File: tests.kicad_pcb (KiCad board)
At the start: 2 copper layers, 30 x 20 mm, 7 parts, among them J101 USB_A+C+XT30

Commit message: ...
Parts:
- moved TP104 2.00 mm to (95.0, 97.0)
- moved TP105 2.00 mm to (95.0, 95.0)
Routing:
- net /SBU1: track 14.8 -> 15.6 mm, vias 0 -> 1
- net /CC2: track 15.2 -> 14.6 mm, vias 1 -> 0

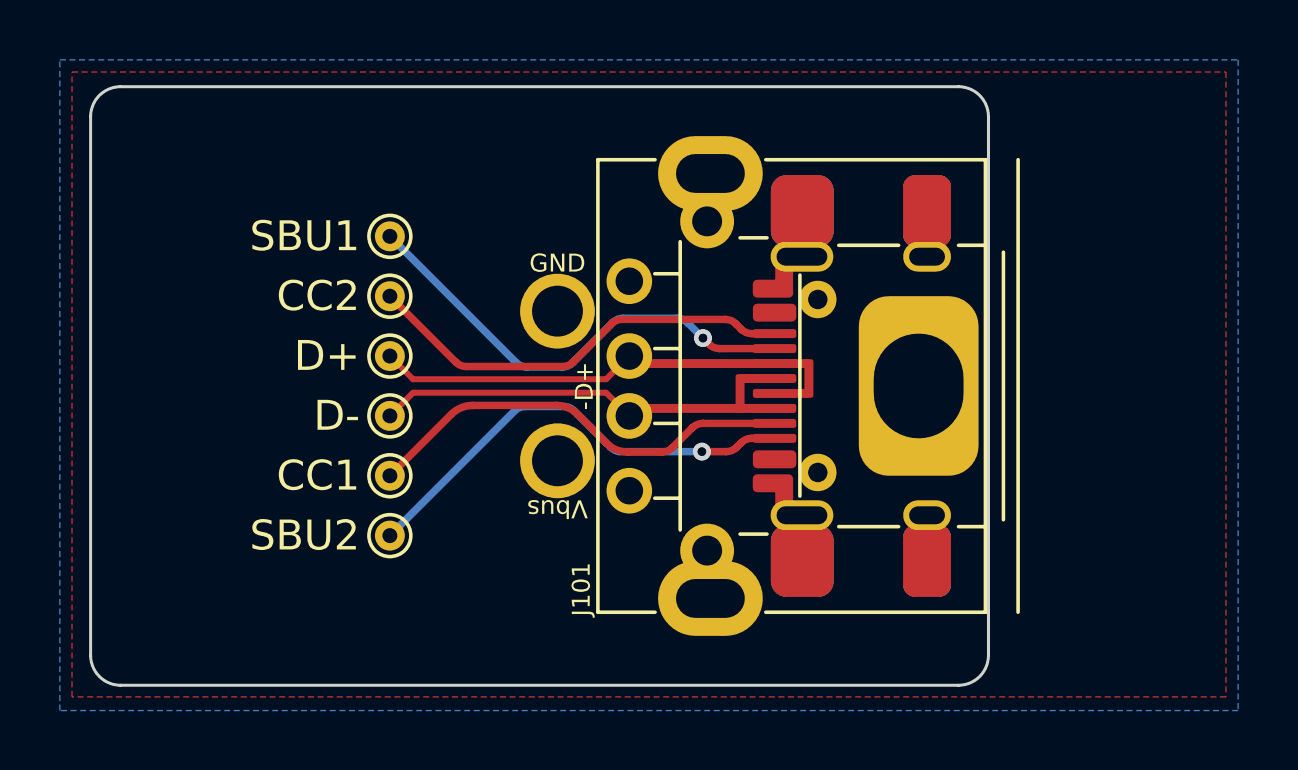
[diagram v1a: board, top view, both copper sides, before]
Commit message: Added tiny Solder Jumpers
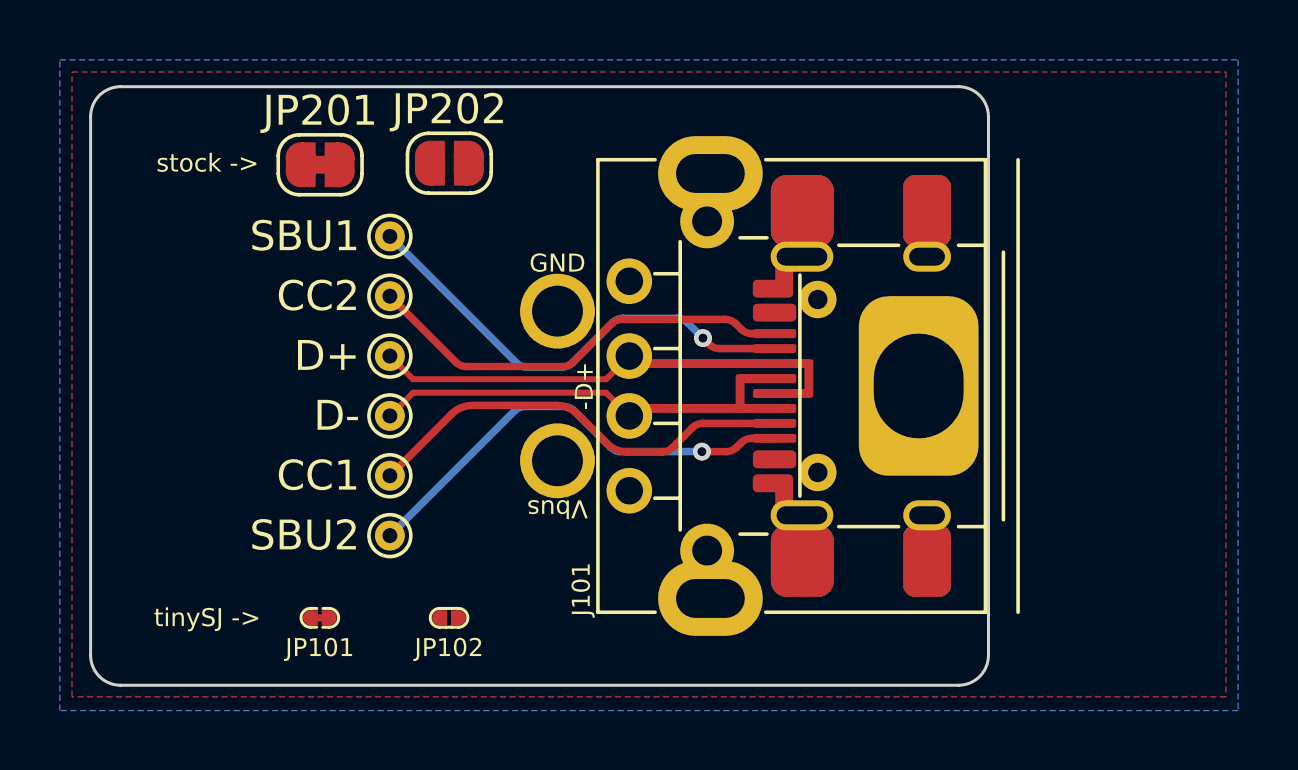
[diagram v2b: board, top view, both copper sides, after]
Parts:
- added JP101: Jumper_2_Bridged, Customs:tinySJ-Bridged, F.Cu at (92.7, 107.7)
- added JP102: Jumper_2_Open, Customs:tinySJ-Open, F.Cu at (97.0, 107.7)
- added JP201: Jumper_2_Bridged, Jumper:SolderJumper-2_P1.3mm_Bridged_RoundedPad1.0x1.5mm, F.Cu at (92.7, 92.6)
- added JP202: Jumper_2_Open, Jumper:SolderJumper-2_P1.3mm_Open_RoundedPad1.0x1.5mm, F.Cu at (97.0, 92.6)
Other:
- board text added: "stock ->"
- board text added: "tinySJ ->"

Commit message: ...
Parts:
- removed JP101: Jumper_2_Bridged, Customs:tinySJ-Bridged
- removed JP102: Jumper_2_Open, Customs:tinySJ-Open
- removed JP201: Jumper_2_Bridged, Jumper:SolderJumper-2_P1.3mm_Bridged_RoundedPad1.0x1.5mm
- removed JP202: Jumper_2_Open, Jumper:SolderJumper-2_P1.3mm_Open_RoundedPad1.0x1.5mm
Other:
- board text removed: "stock ->"
- board text removed: "tinySJ ->"
